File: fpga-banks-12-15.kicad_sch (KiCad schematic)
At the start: 1 part, among them U15 XC7K160T-FFG676

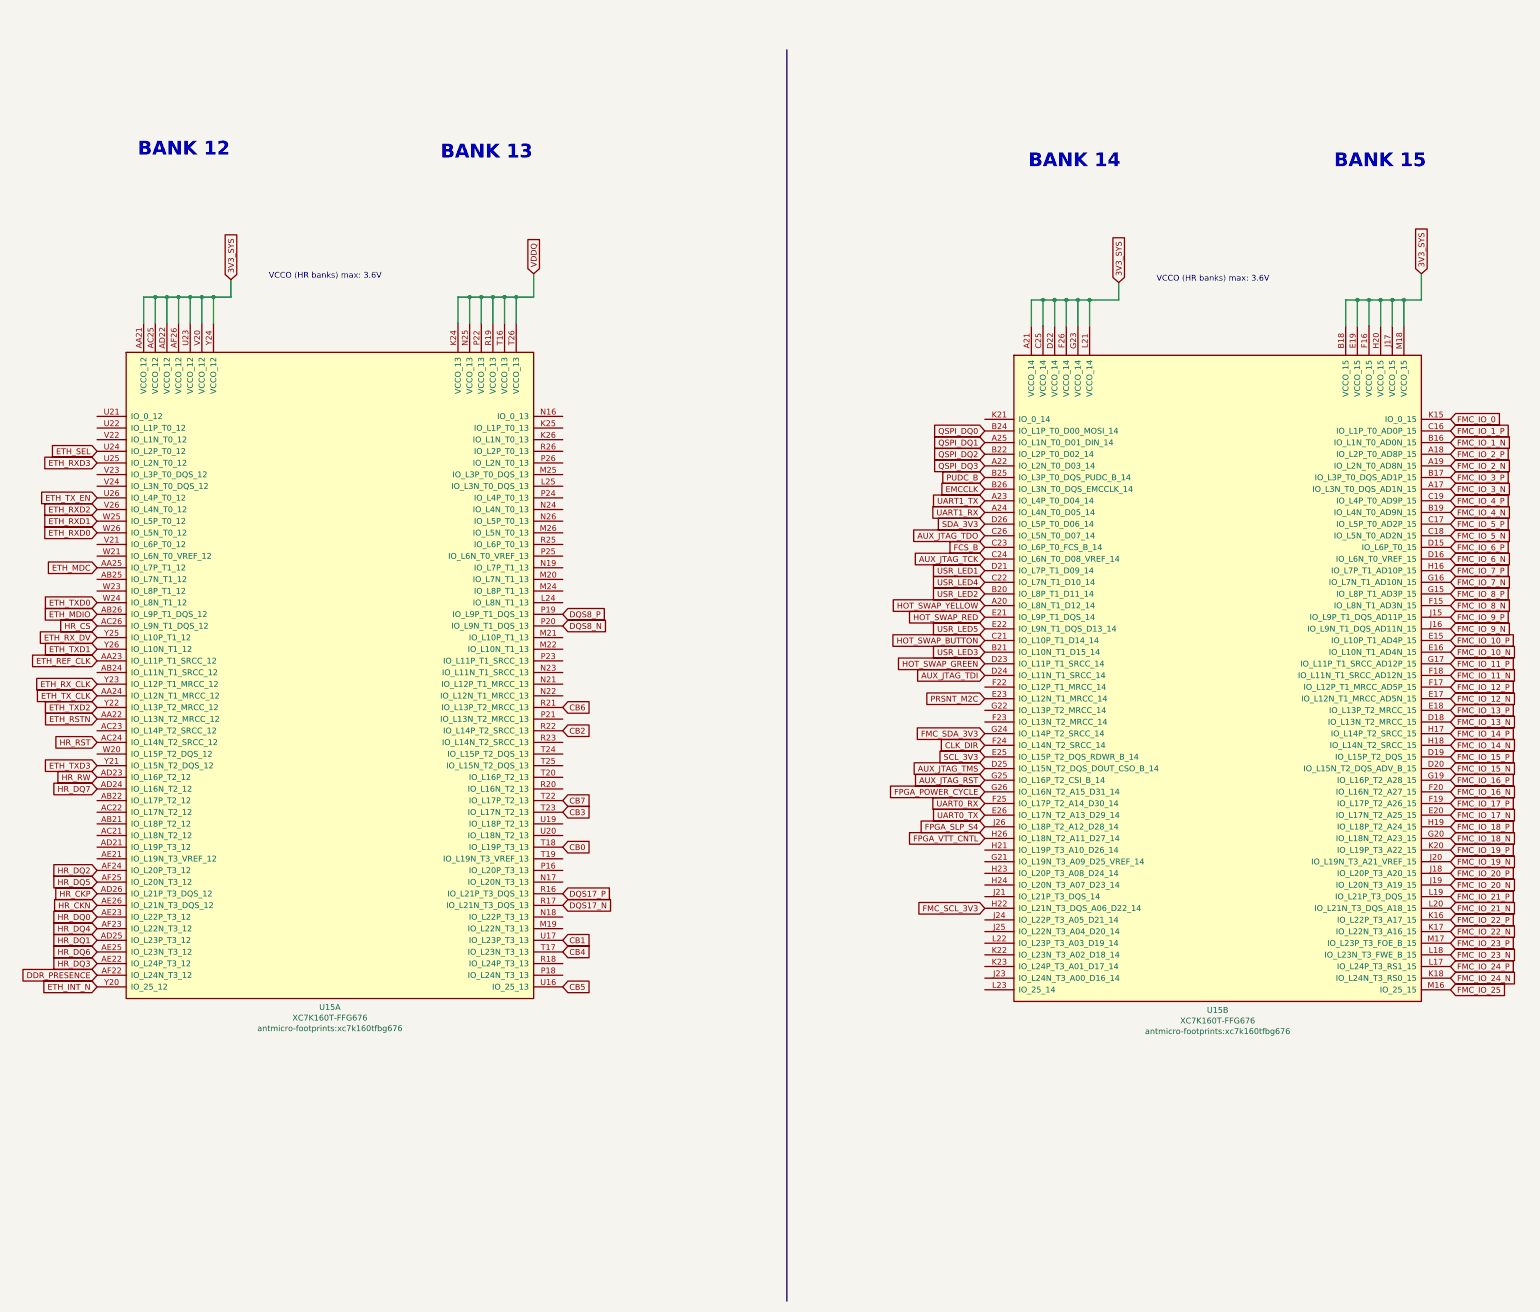
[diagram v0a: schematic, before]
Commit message: Rebase to Rev. 1.2.2
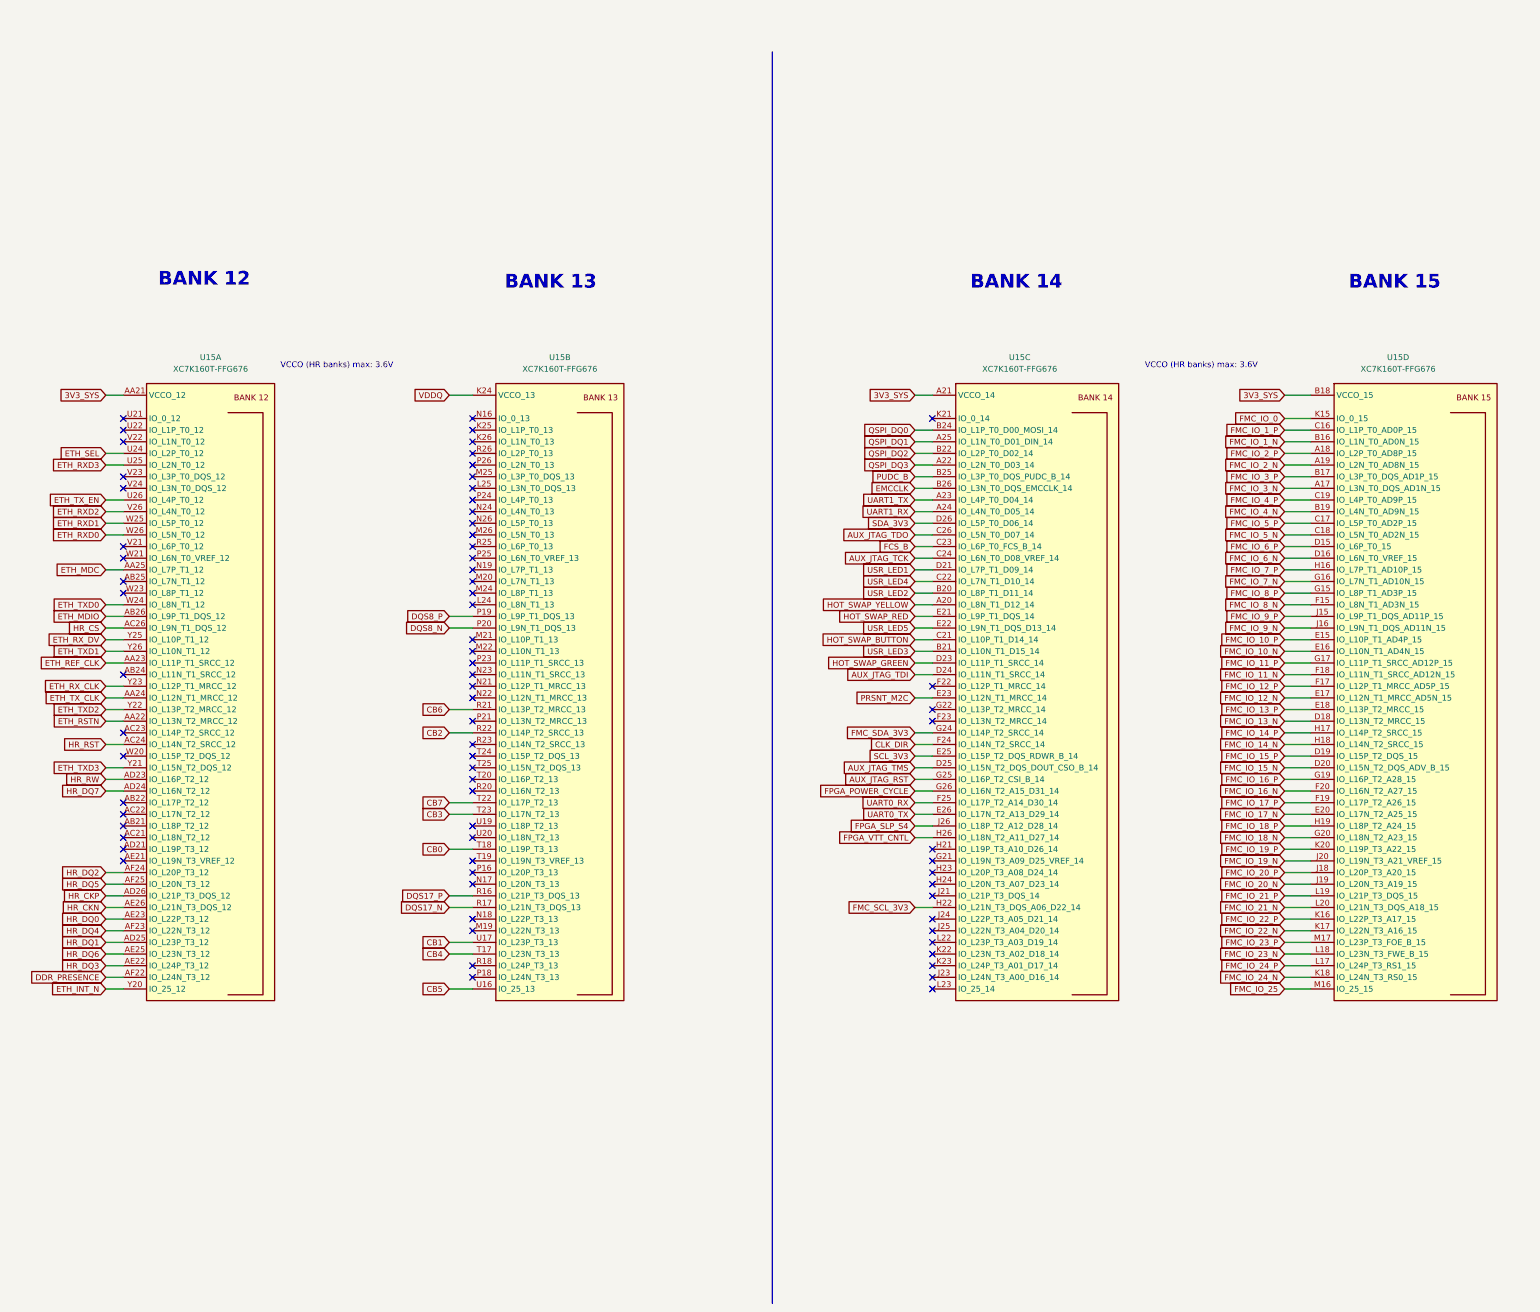
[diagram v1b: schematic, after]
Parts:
- removed U15: XC7K160T-FFG676, antmicro-footprints:xc7k160tfbg676, symbol data-center-dram-tester:XC7K160T-FFG676
- added U15: XC7K160T-FFG676, data-center-rdimm-ddr4-tester-footprints:BGA-676_27x27mm_Layout26x26_P1X1mm, symbol data-center-rdimm-ddr4-tester:XC7K160T-FFG676
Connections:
- net 3V3_SYS: now also U15.A21 (VCCO_14), U15.AA21 (VCCO_12), U15.AC25 (VCCO_12), U15.AD22 (VCCO_12), U15.AF26 (VCCO_12), U15.B18 (VCCO_15), U15.C25 (VCCO_14), U15.D22 (VCCO_14), U15.E19 (VCCO_15), U15.F16 (VCCO_15), U15.F26 (VCCO_14), U15.G23 (VCCO_14), U15.H20 (VCCO_15), U15.J17 (VCCO_15), U15.L21 (VCCO_14), U15.M18 (VCCO_15), U15.U23 (VCCO_12), U15.V20 (VCCO_12), U15.Y24 (VCCO_12)
- net AUX_JTAG_RST: now also U15.G25 (IO_L16P_T2_CSI_B_14)
- net AUX_JTAG_TCK: now also U15.C24 (IO_L6N_T0_D08_VREF_14)
- net AUX_JTAG_TDI: now also U15.D24 (IO_L11N_T1_SRCC_14)
- net AUX_JTAG_TDO: now also U15.C26 (IO_L5N_T0_D07_14)
- net AUX_JTAG_TMS: now also U15.D25 (IO_L15N_T2_DQS_DOUT_CSO_B_14)
- net CB0: now also U15.T18 (IO_L19P_T3_13)
- net CB1: now also U15.U17 (IO_L23P_T3_13)
- net CB2: now also U15.R22 (IO_L14P_T2_SRCC_13)
- net CB3: now also U15.T23 (IO_L17N_T2_13)
- net CB4: now also U15.T17 (IO_L23N_T3_13)
- net CB5: now also U15.U16 (IO_25_13)
- net CB6: now also U15.R21 (IO_L13P_T2_MRCC_13)
- net CB7: now also U15.T22 (IO_L17P_T2_13)
- net CLK_DIR: now also U15.F24 (IO_L14N_T2_SRCC_14)
- net DDR_PRESENCE: now also U15.AF22 (IO_L24N_T3_12)
- net DQS17_N: now also U15.R17 (IO_L21N_T3_DQS_13)
- net DQS17_P: now also U15.R16 (IO_L21P_T3_DQS_13)
- net DQS8_N: now also U15.P20 (IO_L9N_T1_DQS_13)
- net DQS8_P: now also U15.P19 (IO_L9P_T1_DQS_13)
- net EMCCLK: now also U15.B26 (IO_L3N_T0_DQS_EMCCLK_14)
- net ETH_INT_N: now also U15.Y20 (IO_25_12)
- net ETH_MDC: now also U15.AA25 (IO_L7P_T1_12)
- net ETH_MDIO: now also U15.AB26 (IO_L9P_T1_DQS_12)
- net ETH_REF_CLK: now also U15.AA23 (IO_L11P_T1_SRCC_12)
- net ETH_RSTN: now also U15.AA22 (IO_L13N_T2_MRCC_12)
- net ETH_RXD0: now also U15.W26 (IO_L5N_T0_12)
- net ETH_RXD1: now also U15.W25 (IO_L5P_T0_12)
- net ETH_RXD2: now also U15.V26 (IO_L4N_T0_12)
- net ETH_RXD3: now also U15.U25 (IO_L2N_T0_12)
- net ETH_RX_CLK: now also U15.Y23 (IO_L12P_T1_MRCC_12)
- net ETH_RX_DV: now also U15.Y25 (IO_L10P_T1_12)
- net ETH_SEL: now also U15.U24 (IO_L2P_T0_12)
- net ETH_TXD0: now also U15.W24 (IO_L8N_T1_12)
- net ETH_TXD1: now also U15.Y26 (IO_L10N_T1_12)
- net ETH_TXD2: now also U15.Y22 (IO_L13P_T2_MRCC_12)
- net ETH_TXD3: now also U15.Y21 (IO_L15N_T2_DQS_12)
- net ETH_TX_CLK: now also U15.AA24 (IO_L12N_T1_MRCC_12)
- net ETH_TX_EN: now also U15.U26 (IO_L4P_T0_12)
- net FCS_B: now also U15.C23 (IO_L6P_T0_FCS_B_14)
- net FMC_IO_0: now also U15.K15 (IO_0_15)
- net FMC_IO_10_N: now also U15.E16 (IO_L10N_T1_AD4N_15)
- net FMC_IO_10_P: now also U15.E15 (IO_L10P_T1_AD4P_15)
- net FMC_IO_11_N: now also U15.F18 (IO_L11N_T1_SRCC_AD12N_15)
- net FMC_IO_11_P: now also U15.G17 (IO_L11P_T1_SRCC_AD12P_15)
- net FMC_IO_12_N: now also U15.E17 (IO_L12N_T1_MRCC_AD5N_15)
- net FMC_IO_12_P: now also U15.F17 (IO_L12P_T1_MRCC_AD5P_15)
- net FMC_IO_13_N: now also U15.D18 (IO_L13N_T2_MRCC_15)
- net FMC_IO_13_P: now also U15.E18 (IO_L13P_T2_MRCC_15)
- net FMC_IO_14_N: now also U15.H18 (IO_L14N_T2_SRCC_15)
- net FMC_IO_14_P: now also U15.H17 (IO_L14P_T2_SRCC_15)
- net FMC_IO_15_N: now also U15.D20 (IO_L15N_T2_DQS_ADV_B_15)
- net FMC_IO_15_P: now also U15.D19 (IO_L15P_T2_DQS_15)
- net FMC_IO_16_N: now also U15.F20 (IO_L16N_T2_A27_15)
- net FMC_IO_16_P: now also U15.G19 (IO_L16P_T2_A28_15)
- net FMC_IO_17_N: now also U15.E20 (IO_L17N_T2_A25_15)
- net FMC_IO_17_P: now also U15.F19 (IO_L17P_T2_A26_15)
- net FMC_IO_18_N: now also U15.G20 (IO_L18N_T2_A23_15)
- net FMC_IO_18_P: now also U15.H19 (IO_L18P_T2_A24_15)
- net FMC_IO_19_N: now also U15.J20 (IO_L19N_T3_A21_VREF_15)
- net FMC_IO_19_P: now also U15.K20 (IO_L19P_T3_A22_15)
- net FMC_IO_1_N: now also U15.B16 (IO_L1N_T0_AD0N_15)
- net FMC_IO_1_P: now also U15.C16 (IO_L1P_T0_AD0P_15)
- net FMC_IO_20_N: now also U15.J19 (IO_L20N_T3_A19_15)
- net FMC_IO_20_P: now also U15.J18 (IO_L20P_T3_A20_15)
- net FMC_IO_21_N: now also U15.L20 (IO_L21N_T3_DQS_A18_15)
- net FMC_IO_21_P: now also U15.L19 (IO_L21P_T3_DQS_15)
- net FMC_IO_22_N: now also U15.K17 (IO_L22N_T3_A16_15)
- net FMC_IO_22_P: now also U15.K16 (IO_L22P_T3_A17_15)
- net FMC_IO_23_N: now also U15.L18 (IO_L23N_T3_FWE_B_15)
- net FMC_IO_23_P: now also U15.M17 (IO_L23P_T3_FOE_B_15)
- net FMC_IO_24_N: now also U15.K18 (IO_L24N_T3_RS0_15)
- net FMC_IO_24_P: now also U15.L17 (IO_L24P_T3_RS1_15)
- net FMC_IO_25: now also U15.M16 (IO_25_15)
- net FMC_IO_2_N: now also U15.A19 (IO_L2N_T0_AD8N_15)
- net FMC_IO_2_P: now also U15.A18 (IO_L2P_T0_AD8P_15)
- net FMC_IO_3_N: now also U15.A17 (IO_L3N_T0_DQS_AD1N_15)
- net FMC_IO_3_P: now also U15.B17 (IO_L3P_T0_DQS_AD1P_15)
- net FMC_IO_4_N: now also U15.B19 (IO_L4N_T0_AD9N_15)
- net FMC_IO_4_P: now also U15.C19 (IO_L4P_T0_AD9P_15)
- net FMC_IO_5_N: now also U15.C18 (IO_L5N_T0_AD2N_15)
- net FMC_IO_5_P: now also U15.C17 (IO_L5P_T0_AD2P_15)
- net FMC_IO_6_N: now also U15.D16 (IO_L6N_T0_VREF_15)
- net FMC_IO_6_P: now also U15.D15 (IO_L6P_T0_15)
- net FMC_IO_7_N: now also U15.G16 (IO_L7N_T1_AD10N_15)
- net FMC_IO_7_P: now also U15.H16 (IO_L7P_T1_AD10P_15)
- net FMC_IO_8_N: now also U15.F15 (IO_L8N_T1_AD3N_15)
- net FMC_IO_8_P: now also U15.G15 (IO_L8P_T1_AD3P_15)
- net FMC_IO_9_N: now also U15.J16 (IO_L9N_T1_DQS_AD11N_15)
- net FMC_IO_9_P: now also U15.J15 (IO_L9P_T1_DQS_AD11P_15)
- net FMC_SCL_3V3: now also U15.H22 (IO_L21N_T3_DQS_A06_D22_14)
- net FMC_SDA_3V3: now also U15.G24 (IO_L14P_T2_SRCC_14)
- net FPGA_POWER_CYCLE: now also U15.G26 (IO_L16N_T2_A15_D31_14)
- net FPGA_SLP_S4: now also U15.J26 (IO_L18P_T2_A12_D28_14)
- net FPGA_VTT_CNTL: now also U15.H26 (IO_L18N_T2_A11_D27_14)
- net HOT_SWAP_BUTTON: now also U15.C21 (IO_L10P_T1_D14_14)
- net HOT_SWAP_GREEN: now also U15.D23 (IO_L11P_T1_SRCC_14)
- net HOT_SWAP_RED: now also U15.E21 (IO_L9P_T1_DQS_14)
- net HOT_SWAP_YELLOW: now also U15.A20 (IO_L8N_T1_D12_14)
- net HR_CKN: now also U15.AE26 (IO_L21N_T3_DQS_12)
- net HR_CKP: now also U15.AD26 (IO_L21P_T3_DQS_12)
- net HR_CS: now also U15.AC26 (IO_L9N_T1_DQS_12)
- net HR_DQ0: now also U15.AE23 (IO_L22P_T3_12)
- net HR_DQ1: now also U15.AD25 (IO_L23P_T3_12)
- net HR_DQ2: now also U15.AF24 (IO_L20P_T3_12)
- net HR_DQ3: now also U15.AE22 (IO_L24P_T3_12)
- net HR_DQ4: now also U15.AF23 (IO_L22N_T3_12)
- net HR_DQ5: now also U15.AF25 (IO_L20N_T3_12)
- net HR_DQ6: now also U15.AE25 (IO_L23N_T3_12)
- net HR_DQ7: now also U15.AD24 (IO_L16N_T2_12)
- net HR_RST: now also U15.AC24 (IO_L14N_T2_SRCC_12)
- net HR_RW: now also U15.AD23 (IO_L16P_T2_12)
- net PRSNT_M2C: now also U15.E23 (IO_L12N_T1_MRCC_14)
- net PUDC_B: now also U15.B25 (IO_L3P_T0_DQS_PUDC_B_14)
- net QSPI_DQ0: now also U15.B24 (IO_L1P_T0_D00_MOSI_14)
- net QSPI_DQ1: now also U15.A25 (IO_L1N_T0_D01_DIN_14)
- net QSPI_DQ2: now also U15.B22 (IO_L2P_T0_D02_14)
- net QSPI_DQ3: now also U15.A22 (IO_L2N_T0_D03_14)
- net SCL_3V3: now also U15.E25 (IO_L15P_T2_DQS_RDWR_B_14)
- net SDA_3V3: now also U15.D26 (IO_L5P_T0_D06_14)
- net UART0_RX: now also U15.F25 (IO_L17P_T2_A14_D30_14)
- net UART0_TX: now also U15.E26 (IO_L17N_T2_A13_D29_14)
- net UART1_RX: now also U15.A24 (IO_L4N_T0_D05_14)
- net UART1_TX: now also U15.A23 (IO_L4P_T0_D04_14)
- net USR_LED1: now also U15.D21 (IO_L7P_T1_D09_14)
- net USR_LED2: now also U15.B20 (IO_L8P_T1_D11_14)
- net USR_LED3: now also U15.B21 (IO_L10N_T1_D15_14)
- net USR_LED4: now also U15.C22 (IO_L7N_T1_D10_14)
- net USR_LED5: now also U15.E22 (IO_L9N_T1_DQS_D13_14)
- net VDDQ: now also U15.K24 (VCCO_13), U15.N25 (VCCO_13), U15.P22 (VCCO_13), U15.R19 (VCCO_13), U15.T16 (VCCO_13), U15.T26 (VCCO_13)
- no-connect marks 0 -> 72

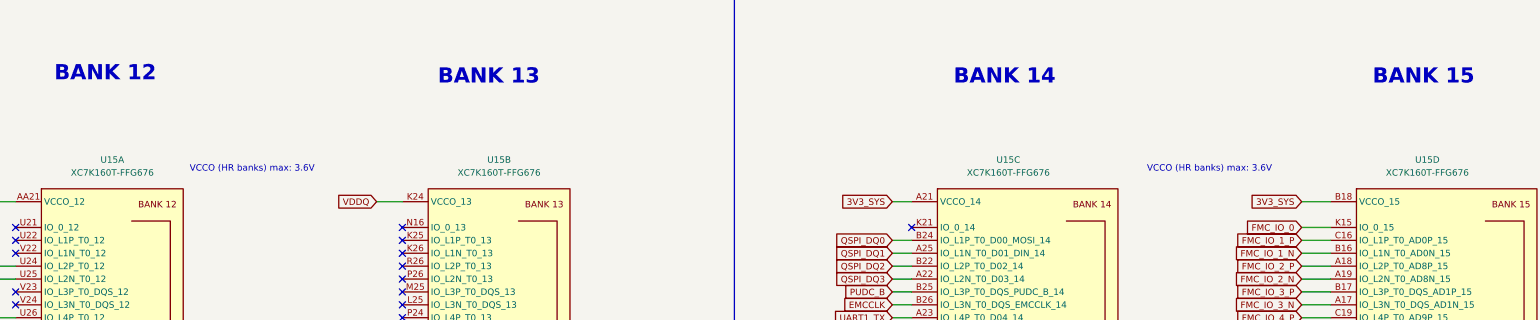
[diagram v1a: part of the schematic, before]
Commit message: Update designators and sync schematic with PCB
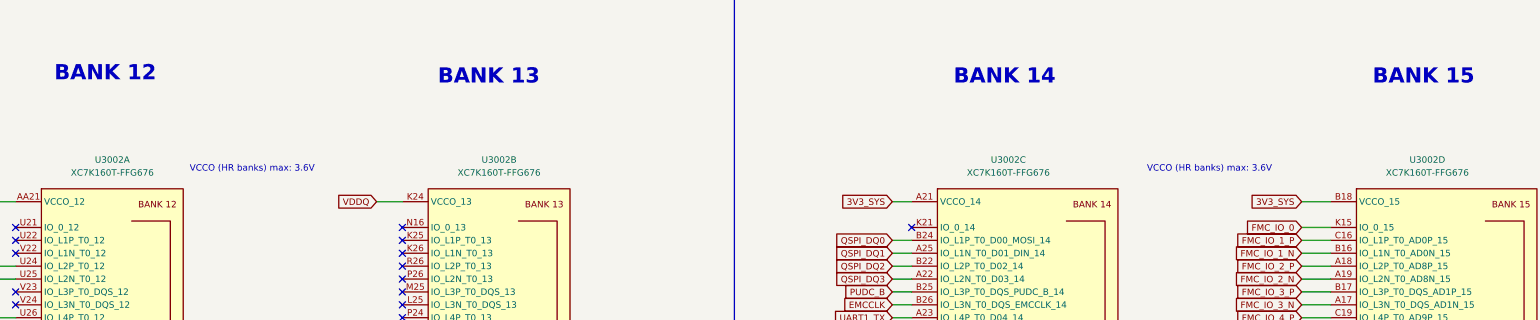
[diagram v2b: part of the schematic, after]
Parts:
- renumbered U15 to U3002
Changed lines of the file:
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@@
   (symbol (lib_id "data-center-rdimm-ddr4-tester:XC7K160T-FFG676") (at 68.58 86.995 0) (unit 1)
     (in_bom yes) (on_board yes) (fields_autoplaced)
-    (property "Reference" "U15" (id 0) (at 87.63 78.74 0))
+    (property "Reference" "U3002" (id 0) (at 87.63 78.74 0))
     (property "Value" "XC7K160T-FFG676" (id 1) (at 87.63 81.28 0)
       (effects (font (size 1.27 1.27) (thickness 0.15)))
@@
   (symbol (lib_id "data-center-rdimm-ddr4-tester:XC7K160T-FFG676") (at 144.78 86.995 0) (unit 2)
     (in_bom yes) (on_board yes) (fields_autoplaced)
-    (property "Reference" "U15" (id 0) (at 163.83 78.74 0))
+    (property "Reference" "U3002" (id 0) (at 163.83 78.74 0))
     (property "Value" "XC7K160T-FFG676" (id 1) (at 163.83 81.28 0)
       (effects (font (size 1.27 1.27) (thickness 0.15)))
@@
   (symbol (lib_id "data-center-rdimm-ddr4-tester:XC7K160T-FFG676") (at 327.66 86.995 0) (unit 4)
     (in_bom yes) (on_board yes) (fields_autoplaced)
-    (property "Reference" "U15" (id 0) (at 346.71 78.74 0))
+    (property "Reference" "U3002" (id 0) (at 346.71 78.74 0))
     (property "Value" "XC7K160T-FFG676" (id 1) (at 346.71 81.28 0)
       (effects (font (size 1.27 1.27) (thickness 0.15)))
@@
   (symbol (lib_id "data-center-rdimm-ddr4-tester:XC7K160T-FFG676") (at 245.11 86.995 0) (unit 3)
     (in_bom yes) (on_board yes) (fields_autoplaced)
-    (property "Reference" "U15" (id 0) (at 264.16 78.74 0))
+    (property "Reference" "U3002" (id 0) (at 264.16 78.74 0))
     (property "Value" "XC7K160T-FFG676" (id 1) (at 264.16 81.28 0)
       (effects (font (size 1.27 1.27) (thickness 0.15)))
